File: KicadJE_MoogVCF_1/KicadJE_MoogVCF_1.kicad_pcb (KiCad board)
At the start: 2 copper layers, 100 x 100 mm, 153 parts, among them J201 CV2, J202 Input2, J203 CV1, J204 Out VCF, J205 Input1, J301 ADSRGate, J302 ADSR, P201 Doepfer_Power_10pin, P301 Doepfer_Power_10pin, Q201 UMX1N, Q202 SS9014, Q203 SS9014, Q204 SS9014, Q205 SS9014, Q206 SS9014, Q207 SS9014, Q208 UMX1N, Q209 UMX1N, Q210 UMX1N, Q211 SS9014, Q212 SS9015, Q301 SI2302, Q302 MMBT3904, Q303 MMBT3904, Q304 MMBT3904, SW301 SW_DPDT_x2, SW302 Gate, U201 TL072, U301 TL072, U302 TLC555

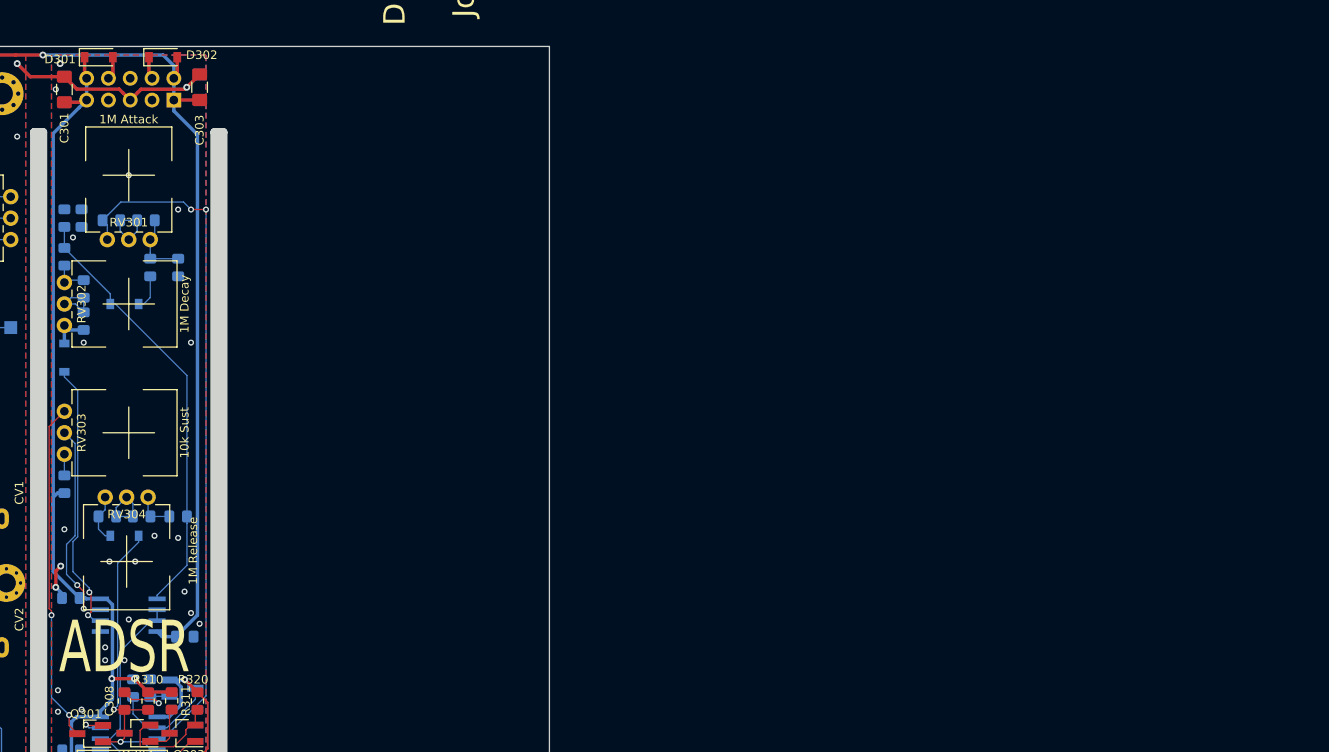
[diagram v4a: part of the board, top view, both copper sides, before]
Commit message: Fix power bug in ADSR TL072
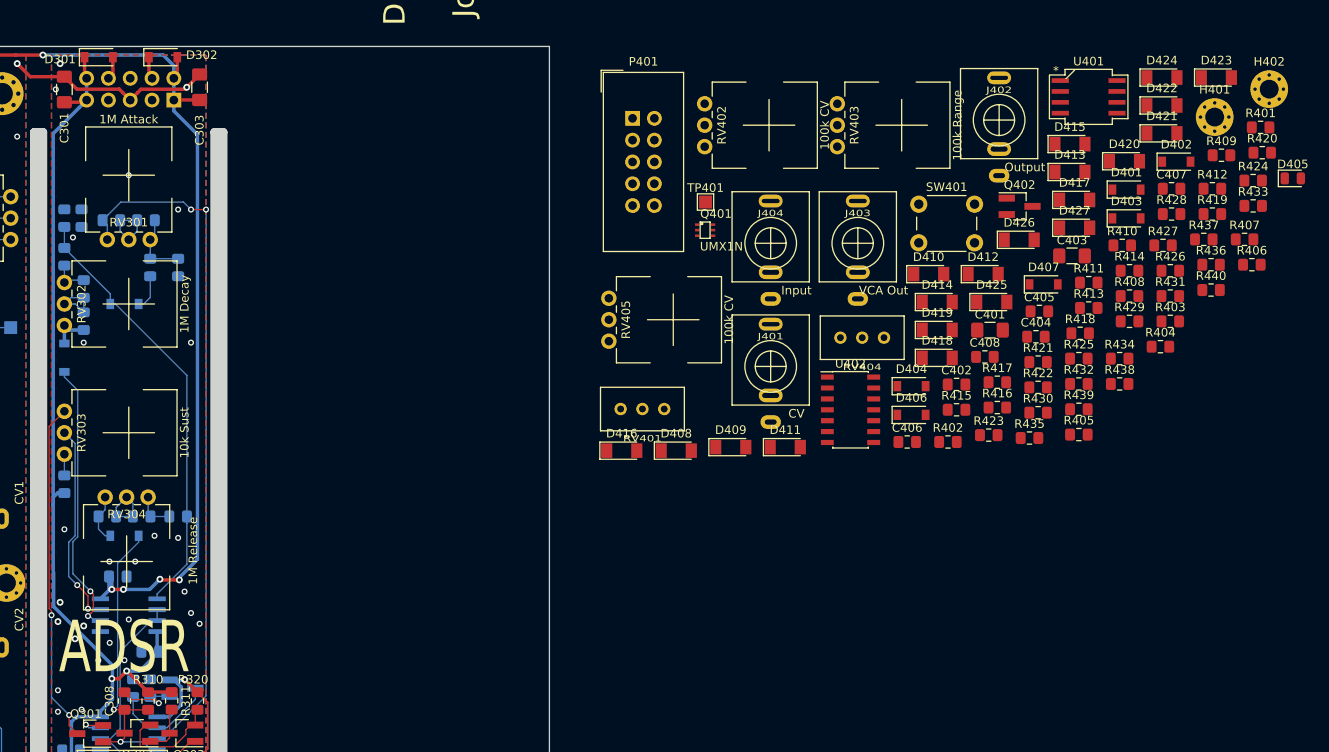
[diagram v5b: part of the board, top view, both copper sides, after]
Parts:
- added C401: 1u, Capacitor_SMD:C_1206_3216Metric_Pad1.42x1.75mm_HandSolder, F.Cu at (201.3, 83.0)
- added C402: 100n, Capacitor_SMD:C_0805_2012Metric_Pad1.15x1.40mm_HandSolder, F.Cu at (197.4, 89.4)
- added C403: 1u, Capacitor_SMD:C_1206_3216Metric_Pad1.42x1.75mm_HandSolder, F.Cu at (210.9, 74.4)
- added C404: 100n, Capacitor_SMD:C_0805_2012Metric_Pad1.15x1.40mm_HandSolder, F.Cu at (206.7, 83.8)
- added C405: 1u/0R, Capacitor_SMD:C_0805_2012Metric_Pad1.15x1.40mm_HandSolder, F.Cu at (207.1, 80.9)
- added C406: 10n opt, Capacitor_SMD:C_0805_2012Metric_Pad1.15x1.40mm_HandSolder, F.Cu at (191.7, 96.1)
- added C407: 10n opt, Capacitor_SMD:C_0805_2012Metric_Pad1.15x1.40mm_HandSolder, F.Cu at (222.5, 66.6)
- added C408: 22u Opt, Capacitor_SMD:C_0805_2012Metric_Pad1.15x1.40mm_HandSolder, F.Cu at (200.7, 86.2)
- added D401: 1N1007, Diode_SMD:D_SOD-123, F.Cu at (217.2, 66.7)
- added D402: 1N1007, Diode_SMD:D_SOD-123, F.Cu at (223.0, 63.4)
- added D403: 1N1007, Diode_SMD:D_SOD-123, F.Cu at (217.2, 70.0)
- added D404: 1N1007, Diode_SMD:D_SOD-123, F.Cu at (192.2, 89.6)
- added D405: LED, LED_SMD:LED_0805_2012Metric, F.Cu at (236.6, 65.4)
- added D406: 1N1007, Diode_SMD:D_SOD-123, F.Cu at (192.2, 92.9)
- added D407: 1N1007, Diode_SMD:D_SOD-123, F.Cu at (207.6, 77.7)
- added D408: LL4148, Diode_SMD:D_MiniMELF, F.Cu at (164.8, 97.1)
- added D409: LL4148, Diode_SMD:D_MiniMELF, F.Cu at (171.1, 96.7)
- added D410: LL4148, Diode_SMD:D_MiniMELF, F.Cu at (194.2, 76.5)
- added D411: LL4148, Diode_SMD:D_MiniMELF, F.Cu at (177.5, 96.7)
- added D412: LL4148, Diode_SMD:D_MiniMELF, F.Cu at (200.5, 76.5)
- added D413: LL4148, Diode_SMD:D_MiniMELF, F.Cu at (210.6, 64.6)
- added D414: LL4148, Diode_SMD:D_MiniMELF, F.Cu at (195.2, 79.8)
- added D415: LL4148, Diode_SMD:D_MiniMELF, F.Cu at (210.6, 61.4)
- added D416: LL4148, Diode_SMD:D_MiniMELF, F.Cu at (158.4, 97.1)
- added D417: LL4148, Diode_SMD:D_MiniMELF, F.Cu at (211.2, 67.9)
- added D418: LL4148, Diode_SMD:D_MiniMELF, F.Cu at (195.2, 86.3)
- added D419: LL4148, Diode_SMD:D_MiniMELF, F.Cu at (195.2, 83.0)
- added D420: LL4148, Diode_SMD:D_MiniMELF, F.Cu at (217.0, 63.4)
- added D421: LL4148, Diode_SMD:D_MiniMELF, F.Cu at (221.3, 60.1)
- added D422: LL4148, Diode_SMD:D_MiniMELF, F.Cu at (221.3, 56.9)
- added D423: LL4148, Diode_SMD:D_MiniMELF, F.Cu at (227.7, 53.6)
- added D424: LL4148, Diode_SMD:D_MiniMELF, F.Cu at (221.3, 53.6)
- added D425: LL4148, Diode_SMD:D_MiniMELF, F.Cu at (201.5, 79.8)
- added D426: LL4148, Diode_SMD:D_MiniMELF, F.Cu at (204.7, 72.5)
- added D427: LL4148, Diode_SMD:D_MiniMELF, F.Cu at (211.2, 71.1)
- added H401: 2,2mm, MountingHole:MountingHole_2.2mm_M2_Pad_Via, F.Cu at (227.5, 58.2)
- added H402: 2,2mm, MountingHole:MountingHole_2.2mm_M2_Pad_Via, F.Cu at (233.8, 55.0)
- added J401: CV, AJ-Dropbox-Kicad:PJ301SM, F.Cu at (175.8, 87.3)
- added J402: Output, AJ-Dropbox-Kicad:PJ301SM, F.Cu at (202.4, 58.6)
- added J403: VCA Out, AJ-Dropbox-Kicad:PJ301SM, F.Cu at (185.9, 72.9)
- added J404: Input, AJ-Dropbox-Kicad:PJ301SM, F.Cu at (175.8, 72.9)
- added P401: Doepfer_Power_10pin, Connectors_IDC:IDC-Header_2x05_Pitch2.54mm_Straight, F.Cu at (159.7, 58.4)
- added Q401: UMX1N, AJ:UMX1N_UMT6_DualNPN, F.Cu at (168.1, 71.4)
- added Q402: SS9014, Package_TO_SOT_SMD:SOT-23_Handsoldering, F.Cu at (204.8, 68.6)
- added R401: 47k, Resistor_SMD:R_0805_2012Metric_Pad1.15x1.40mm_HandSolder, F.Cu at (232.8, 59.4)
- added R402: 470R, Resistor_SMD:R_0805_2012Metric_Pad1.15x1.40mm_HandSolder, F.Cu at (196.4, 96.1)
- added R403: 12K, Resistor_SMD:R_0805_2012Metric_Pad1.15x1.40mm_HandSolder, F.Cu at (222.3, 82.0)
- added R404: 470R, Resistor_SMD:R_0805_2012Metric_Pad1.15x1.40mm_HandSolder, F.Cu at (221.2, 85.0)
- added R405: 47k, Resistor_SMD:R_0805_2012Metric_Pad1.15x1.40mm_HandSolder, F.Cu at (211.7, 95.2)
- added R406: 5k6, Resistor_SMD:R_0805_2012Metric_Pad1.15x1.40mm_HandSolder, F.Cu at (231.8, 75.4)
- added R407: 15k 1%, Resistor_SMD:R_0805_2012Metric_Pad1.15x1.40mm_HandSolder, F.Cu at (231.0, 72.5)
- added R408: 15k 1%, Resistor_SMD:R_0805_2012Metric_Pad1.15x1.40mm_HandSolder, F.Cu at (217.6, 79.1)
- added R409: 100k 1%, Resistor_SMD:R_0805_2012Metric_Pad1.15x1.40mm_HandSolder, F.Cu at (228.3, 62.7)
- added R410: 10k 1%, Resistor_SMD:R_0805_2012Metric_Pad1.15x1.40mm_HandSolder, F.Cu at (216.7, 73.2)
- added R411: 5k6, Resistor_SMD:R_0805_2012Metric_Pad1.15x1.40mm_HandSolder, F.Cu at (212.8, 77.5)
- added R412: 100k, Resistor_SMD:R_0805_2012Metric_Pad1.15x1.40mm_HandSolder, F.Cu at (227.2, 66.6)
- added R413: 10k 1%, Resistor_SMD:R_0805_2012Metric_Pad1.15x1.40mm_HandSolder, F.Cu at (212.8, 80.5)
- added R414: 680R, Resistor_SMD:R_0805_2012Metric_Pad1.15x1.40mm_HandSolder, F.Cu at (217.6, 76.1)
- added R415: 100k 1%, Resistor_SMD:R_0805_2012Metric_Pad1.15x1.40mm_HandSolder, F.Cu at (197.4, 92.3)
- added R416: 15k, Resistor_SMD:R_0805_2012Metric_Pad1.15x1.40mm_HandSolder, F.Cu at (202.2, 92.1)
- added R417: 68k, Resistor_SMD:R_0805_2012Metric_Pad1.15x1.40mm_HandSolder, F.Cu at (202.2, 89.1)
- added R418: 100k, Resistor_SMD:R_0805_2012Metric_Pad1.15x1.40mm_HandSolder, F.Cu at (211.8, 83.4)
- added R419: 15k, Resistor_SMD:R_0805_2012Metric_Pad1.15x1.40mm_HandSolder, F.Cu at (227.2, 69.5)
- added R420: 33k, Resistor_SMD:R_0805_2012Metric_Pad1.15x1.40mm_HandSolder, F.Cu at (233.0, 62.4)
- added R421: 22k, Resistor_SMD:R_0805_2012Metric_Pad1.15x1.40mm_HandSolder, F.Cu at (206.9, 86.8)
- added R422: 100k, Resistor_SMD:R_0805_2012Metric_Pad1.15x1.40mm_HandSolder, F.Cu at (206.9, 89.7)
- added R423: 22k, Resistor_SMD:R_0805_2012Metric_Pad1.15x1.40mm_HandSolder, F.Cu at (201.2, 95.3)
- added R424: 15k, Resistor_SMD:R_0805_2012Metric_Pad1.15x1.40mm_HandSolder, F.Cu at (232.0, 65.6)
- added R425: 15k, Resistor_SMD:R_0805_2012Metric_Pad1.15x1.40mm_HandSolder, F.Cu at (211.7, 86.4)
- added R426: 56k, Resistor_SMD:R_0805_2012Metric_Pad1.15x1.40mm_HandSolder, F.Cu at (222.3, 76.1)
- added R427: 15k, Resistor_SMD:R_0805_2012Metric_Pad1.15x1.40mm_HandSolder, F.Cu at (221.5, 73.2)
- added R428: 27k, Resistor_SMD:R_0805_2012Metric_Pad1.15x1.40mm_HandSolder, F.Cu at (222.5, 69.5)
- added R429: 15k, Resistor_SMD:R_0805_2012Metric_Pad1.15x1.40mm_HandSolder, F.Cu at (217.6, 82.0)
- added R430: 56k, Resistor_SMD:R_0805_2012Metric_Pad1.15x1.40mm_HandSolder, F.Cu at (206.9, 92.7)
- added R431: 15k, Resistor_SMD:R_0805_2012Metric_Pad1.15x1.40mm_HandSolder, F.Cu at (222.3, 79.1)
- added R432: 0R, Resistor_SMD:R_0805_2012Metric_Pad1.15x1.40mm_HandSolder, F.Cu at (211.7, 89.3)
- added R433: 5k6, Resistor_SMD:R_0805_2012Metric_Pad1.15x1.40mm_HandSolder, F.Cu at (232.0, 68.6)
- added R434: 15k, Resistor_SMD:R_0805_2012Metric_Pad1.15x1.40mm_HandSolder, F.Cu at (216.4, 86.4)
- added R435: Open, Resistor_SMD:R_0805_2012Metric_Pad1.15x1.40mm_HandSolder, F.Cu at (205.9, 95.6)
- added R436: 2k7, Resistor_SMD:R_0805_2012Metric_Pad1.15x1.40mm_HandSolder, F.Cu at (227.1, 75.4)
- added R437: 33k, Resistor_SMD:R_0805_2012Metric_Pad1.15x1.40mm_HandSolder, F.Cu at (226.2, 72.5)
- added R438: 15k, Resistor_SMD:R_0805_2012Metric_Pad1.15x1.40mm_HandSolder, F.Cu at (216.4, 89.3)
- added R439: 100k, Resistor_SMD:R_0805_2012Metric_Pad1.15x1.40mm_HandSolder, F.Cu at (211.7, 92.3)
- added R440: 100k, Resistor_SMD:R_0805_2012Metric_Pad1.15x1.40mm_HandSolder, F.Cu at (227.1, 78.4)
- added RV401: 1k, AJ-Dropbox-Kicad:Bourns3296WV, F.Cu at (163.4, 92.2)
- added RV402: 100k CV, Potentiometer_THT:Potentiometer_China_RK09_Single_Vertical_AJ, F.Cu at (168.1, 61.7)
- added RV403: 100k Range, Potentiometer_THT:Potentiometer_China_RK09_Single_Vertical_AJ, F.Cu at (183.5, 61.7)
- added RV404: 50k, AJ-Dropbox-Kicad:Bourns3296WV, F.Cu at (189.0, 83.9)
- added RV405: 100k CV, Potentiometer_THT:Potentiometer_China_RK09_Single_Vertical_AJ, F.Cu at (156.9, 84.3)
- added SW401: Gate, Button_Switch_THT:SW_PUSH_6mm, F.Cu at (193.0, 68.4)
- added TP401: Input, TestPoint:TestPoint_Pad_1.5x1.5mm, F.Cu at (168.2, 68.1)
- added U401: TL072, AJ-Dropbox-Kicad:AJ_SO-8_5.3x6.2mm_P1.27mm, F.Cu at (212.8, 55.9)
- added U402: TL074, Package_SO:SOIC-14_3.9x8.7mm_P1.27mm, F.Cu at (185.1, 92.3)
- moved C302 11.2 mm to (103.5, 120.5)
- moved C304 10.5 mm to (99.7, 111.8)
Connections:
- C306 pad 2: Net-(C306-Pad2) -> (no net)
- R304 pad 2: Net-(R304-Pad2) -> (no net)
- U301 pad 4: +12V -> -12V
- U301 pad 8: -12V -> +12V
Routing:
- net +12V: track 249.9 -> 257.2 mm
- net GND: track 142.3 -> 138.1 mm, vias 42 -> 44
- net -12V: track 215.4 -> 219.3 mm, vias 1 -> 5
- net Net-(RV303-Pad2): track 24.3 -> 23.8 mm

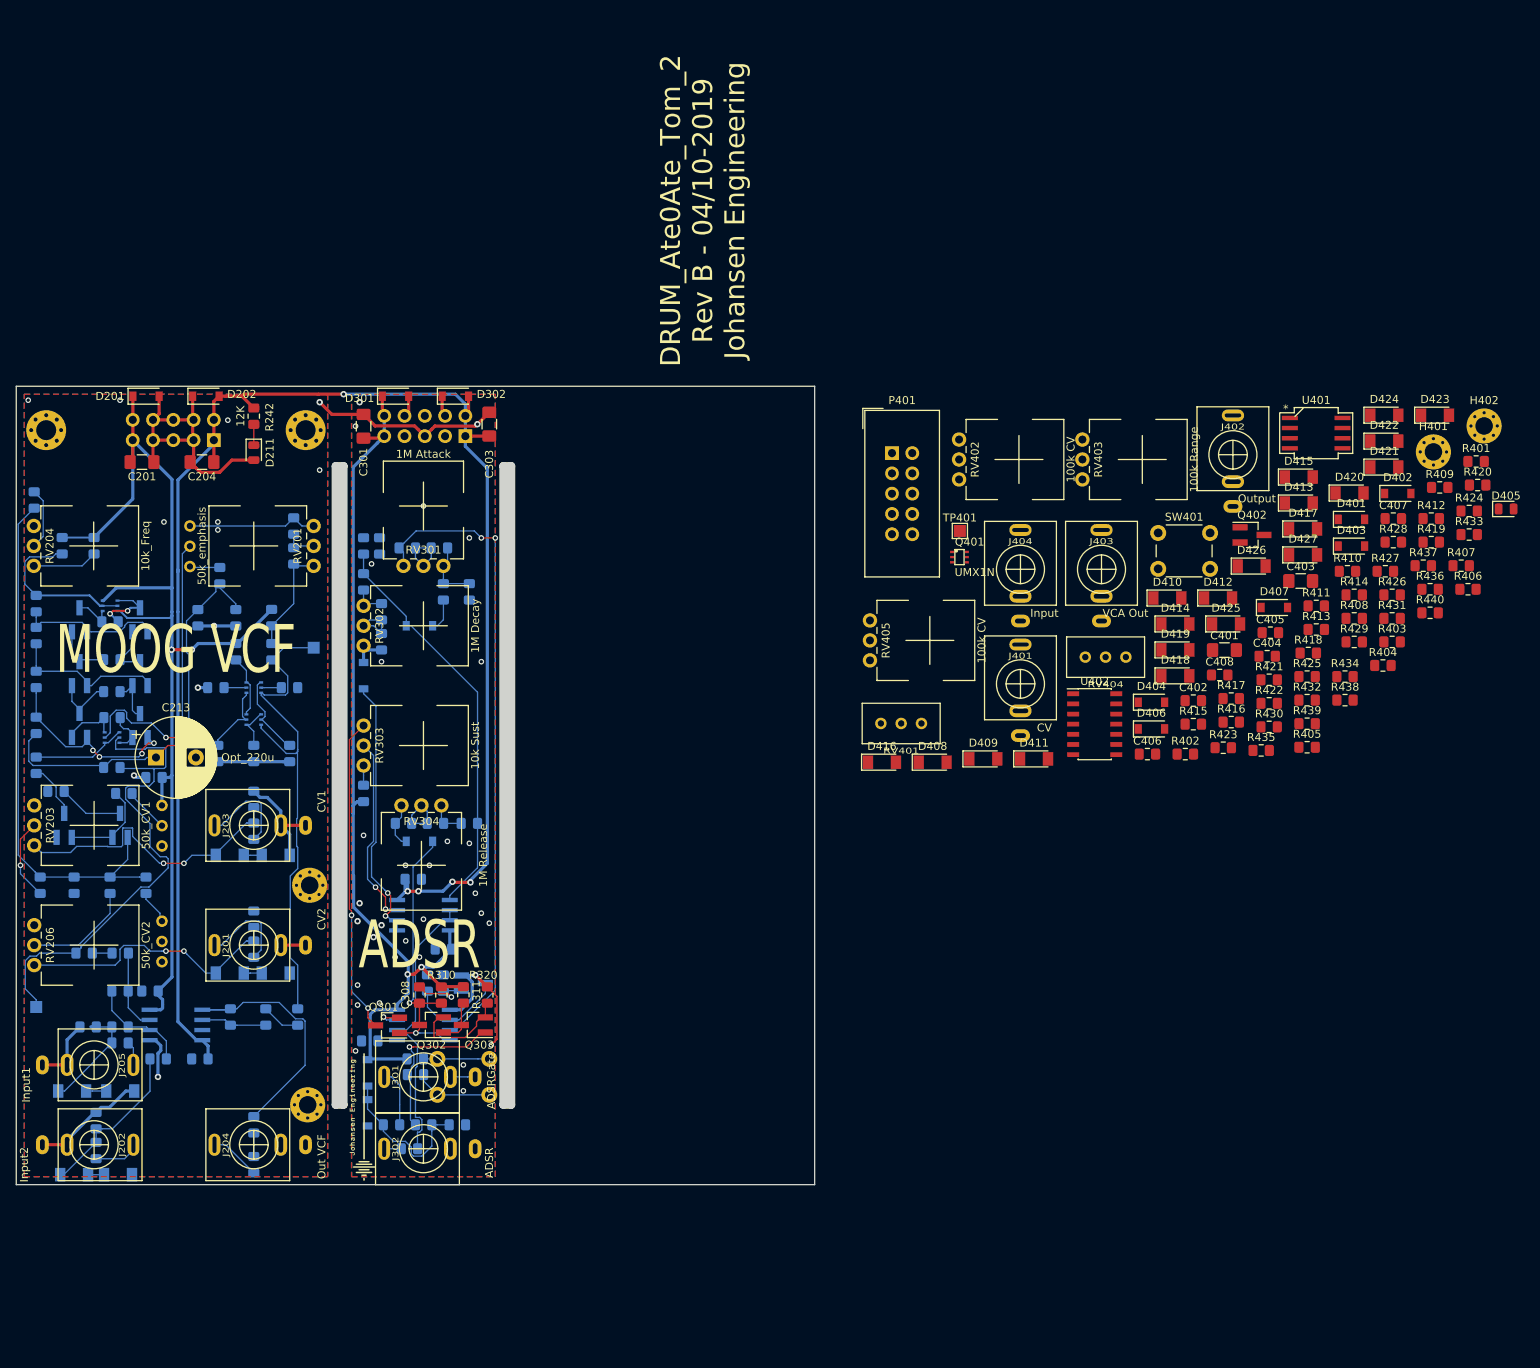
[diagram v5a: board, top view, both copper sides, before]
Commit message: Folding Diode conn missing
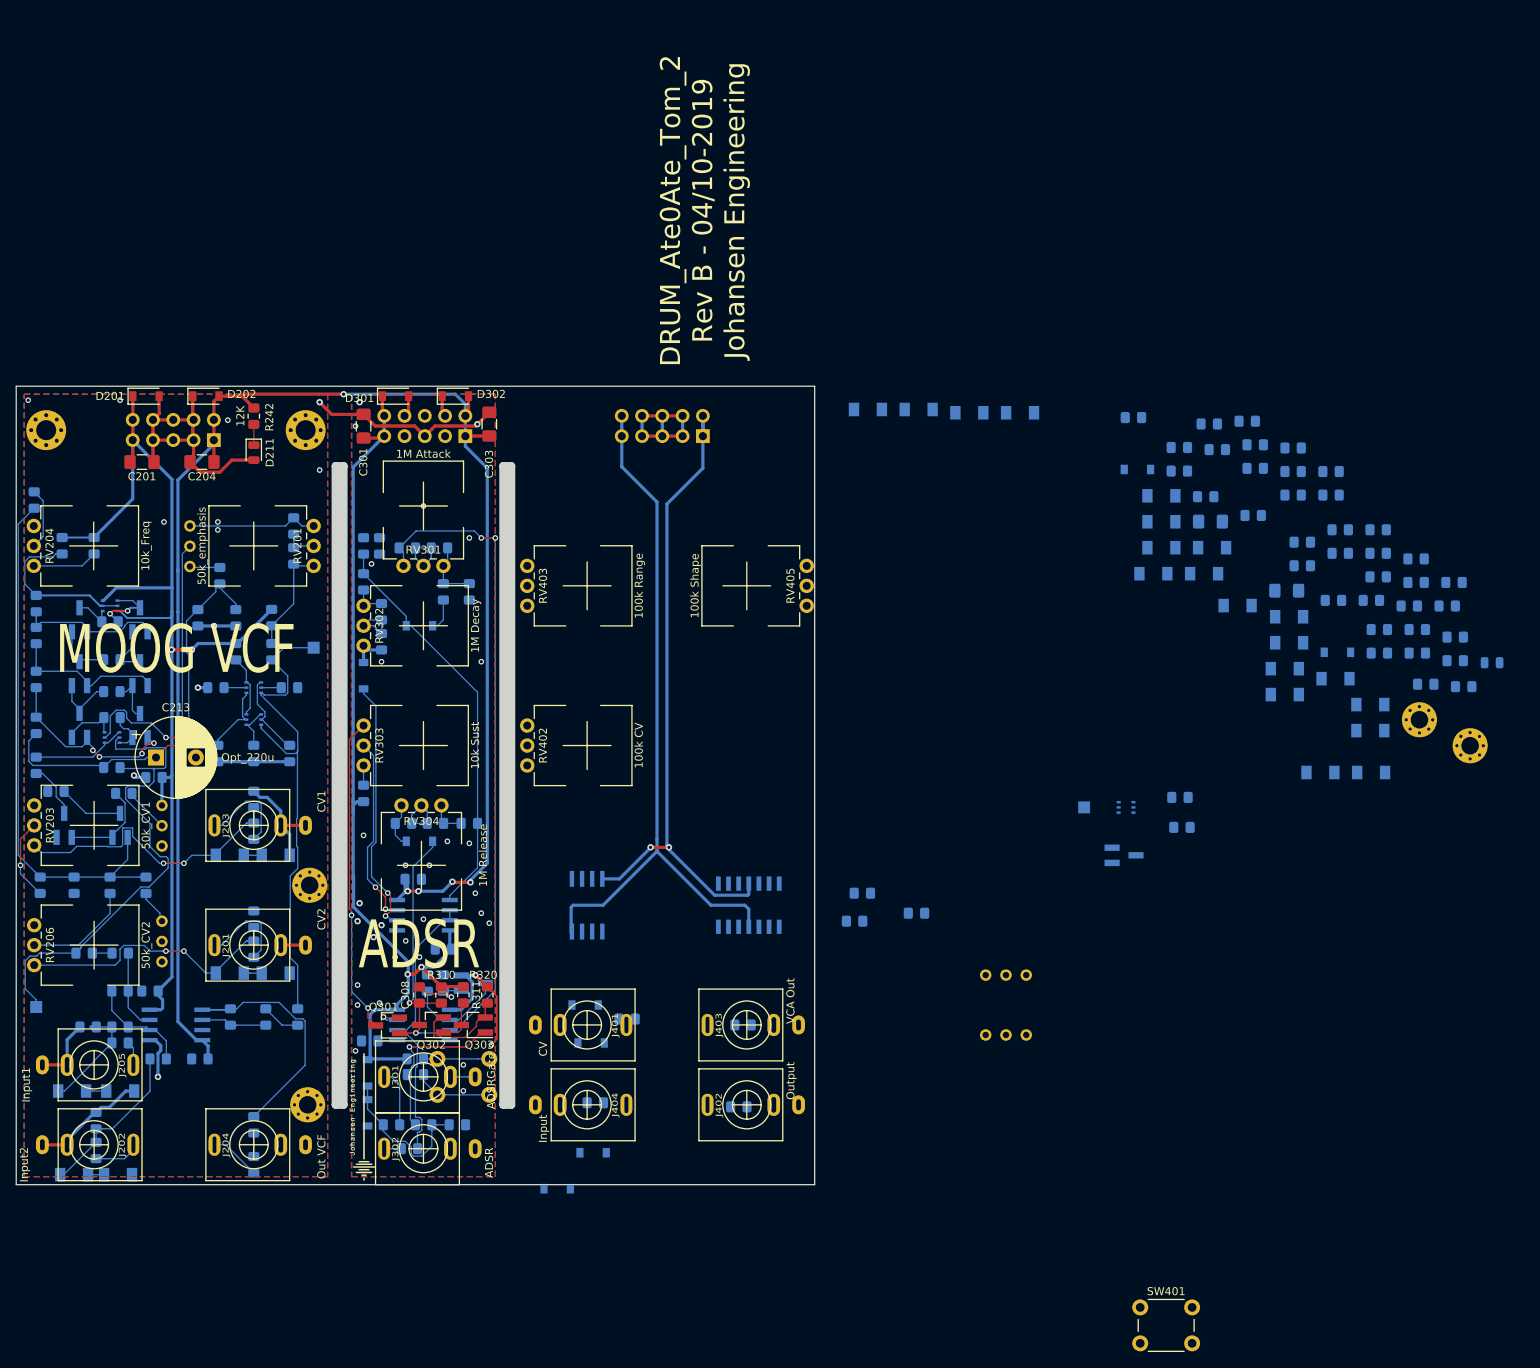
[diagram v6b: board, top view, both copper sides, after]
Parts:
- C401, C402, C403, C404, C405, C406, C407, C408, D401, D402, D403, D404, D405, D406, D407, D408, D409, D410, D411, D412, D413, D414, D415, D416, D417, D418, D419, D420, D421, D422, D423, D424, D425, D426, D427, H401, H402, P401, Q401, Q402, R401, R402, R403, R404, R405, R406, R407, R408, R409, R410, R411, R412, R413, R414, R415, R416, R417, R418, R419, R420, R421, R422, R423, R424, R425, R426, R427, R428, R429, R430, R431, R432, R433, R434, R435, R436, R437, R438, R439, R440, RV401, RV404, TP401, U401: moved to B.Cu
- RV405: value 100k CV -> 100k Shape
- U402: footprint Package_SO:SOIC-14_3.9x8.7mm_P1.27mm -> AJ:SOIC-14_3.9x8.7mm_P1.27mm; moved to B.Cu
- moved R401 127.2 mm to (126.5, 129.2)
- moved D402 122.2 mm to (122.0, 132.2)
- moved D403 111.9 mm to (121.2, 127.5)
- moved D407 109.3 mm to (122.2, 146.0)
- moved U401 108.8 mm to (121.5, 115.0), turned to 270 degrees
- moved J402 101.7 mm to (141.5, 140.0), turned to 90 degrees
- moved R405 99.7 mm to (122.5, 139.8)
- moved SW401 97.0 mm to (190.8, 165.4)
- moved D406 94.1 mm to (117.8, 150.5)
- moved R404 91.9 mm to (141.0, 130.0)
- moved J404 86.3 mm to (121.5, 140.0), turned to 270 degrees
- moved J403 72.3 mm to (141.5, 130.0), turned to 90 degrees
- moved RV403 71.3 mm to (114.0, 77.5)
- moved R402 71.3 mm to (140.5, 140.2)
- moved J401 69.1 mm to (121.5, 130.0), turned to 270 degrees
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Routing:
- net +12V: track 257.2 -> 347.0 mm
- net -12V: track 219.3 -> 302.2 mm, vias 5 -> 7
- net GND: track 138.1 -> 155.9 mm
